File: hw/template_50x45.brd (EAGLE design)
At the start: 50 x 45 mm, 23 parts, among them J1 GROVE-4P-2.0-3470130P1, J2 GROVE-4P-2.0-3470130P1

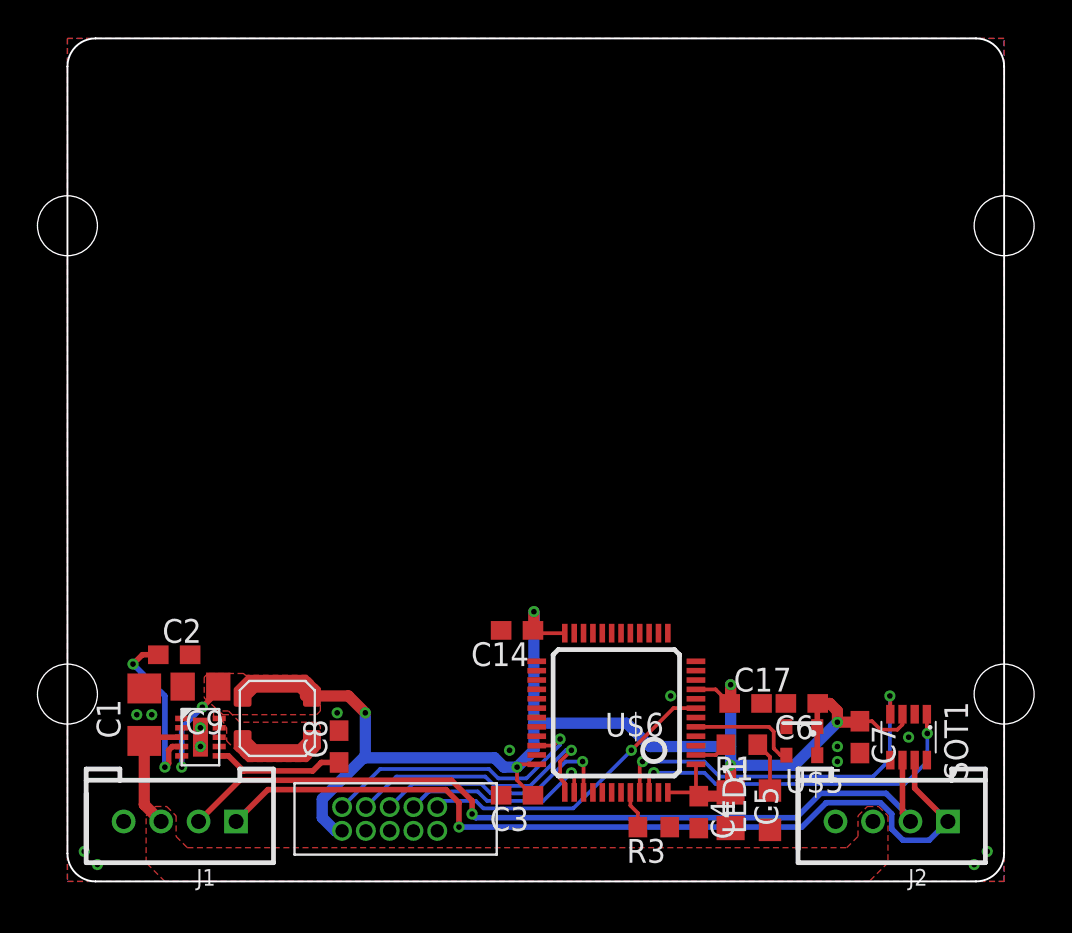
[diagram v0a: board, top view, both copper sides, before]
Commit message: Updated to R2P Eagle libraries
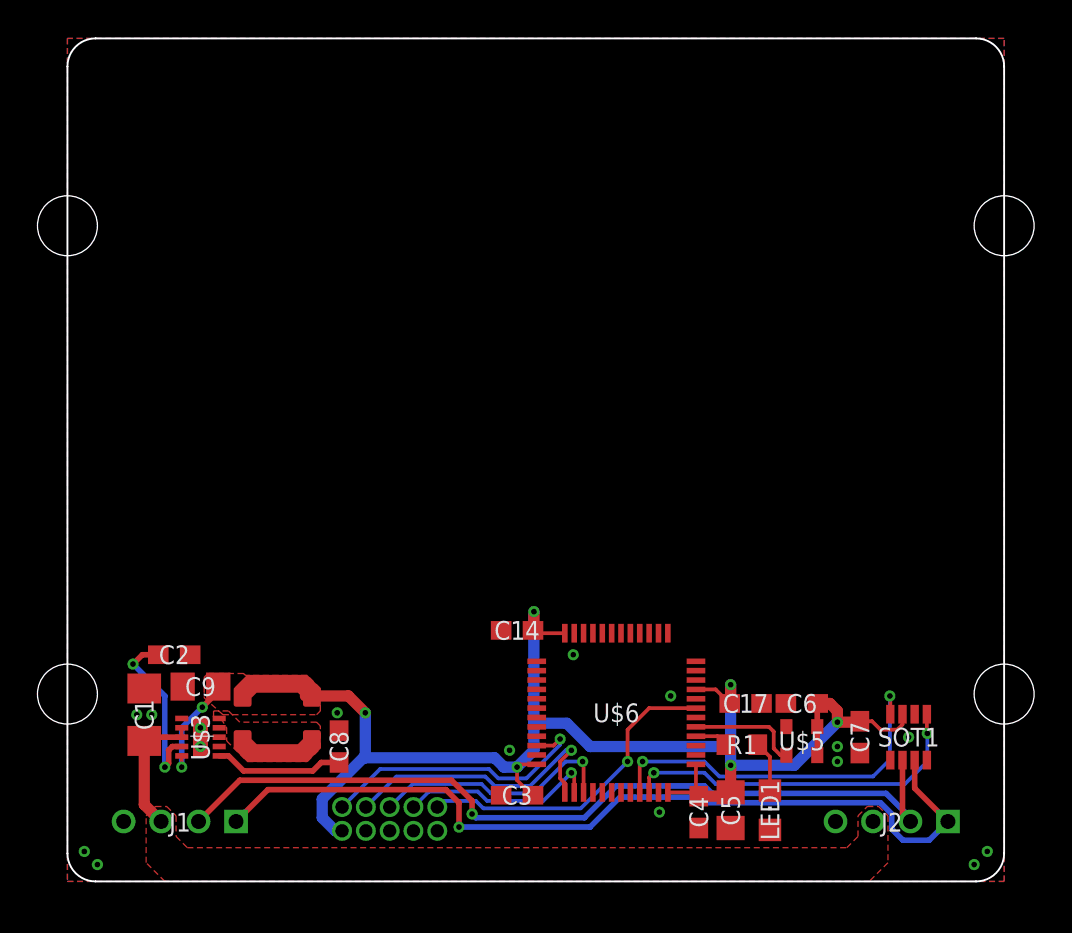
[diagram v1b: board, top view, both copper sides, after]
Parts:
- removed R3: 10k, rcl:R0603
- C1: value (none) -> 1u; device rcl:C1206 -> r2p_rcl:C1206
- C14, C17, C2, C3, C4, C6, C7, C8: device rcl:C0603 -> r2p_rcl:C0603
- C5: device rcl:C0805 -> r2p_rcl:C0805
- C9: value (none) -> 10u; device rcl:C0805 -> r2p_rcl:C0805
- J1, J2: value GROVE-4P-2.0-3470130P1 -> R2P_BUS-VERTICAL; device OPL Eagle Library:4P-2.0 -> r2p_connector:OPL-EAGLE-LIBRARY_4P-2.0
- LED1: device led:CHIPLED_0805 -> r2p_led:CHIPLED_0805
- R1: device rcl:R0603 -> r2p_rcl:R0603
- SOT1: device maxim:SOT23-8L -> r2p_ic:SOT23-8L
- U$2: device coilcraft:LPS4018 -> r2p_rcl:COILCRAFT_LPS4018
- U$3: device maxim:TDFN-10 -> r2p_ic:TDFN-10
- U$4: value FTSH-105TH -> JTAG-TH; device samtec:FTSH-105-TH -> r2p_connector:SAMTEC_FTSH-105-TH
- U$5: value ASD -> ABRACON_ASD; device abracon:2.5X2 -> r2p_ic:ABRACON_2.5X2
- U$6: value STM32F303C -> STM32F303CTX; device st:LQFP48 -> r2p_ic:LQFP48
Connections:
- net VIN renamed +VBUS
- removed net BOOT0: R3.2, U$6.44
- net GND: now also U$6.44; no longer R3.1
- net LED1: now also U$6.4; no longer U$6.2
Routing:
- net BOOT0: track 2.02 -> 0.00 mm
- net NRST: track 16.3 -> 17.3 mm

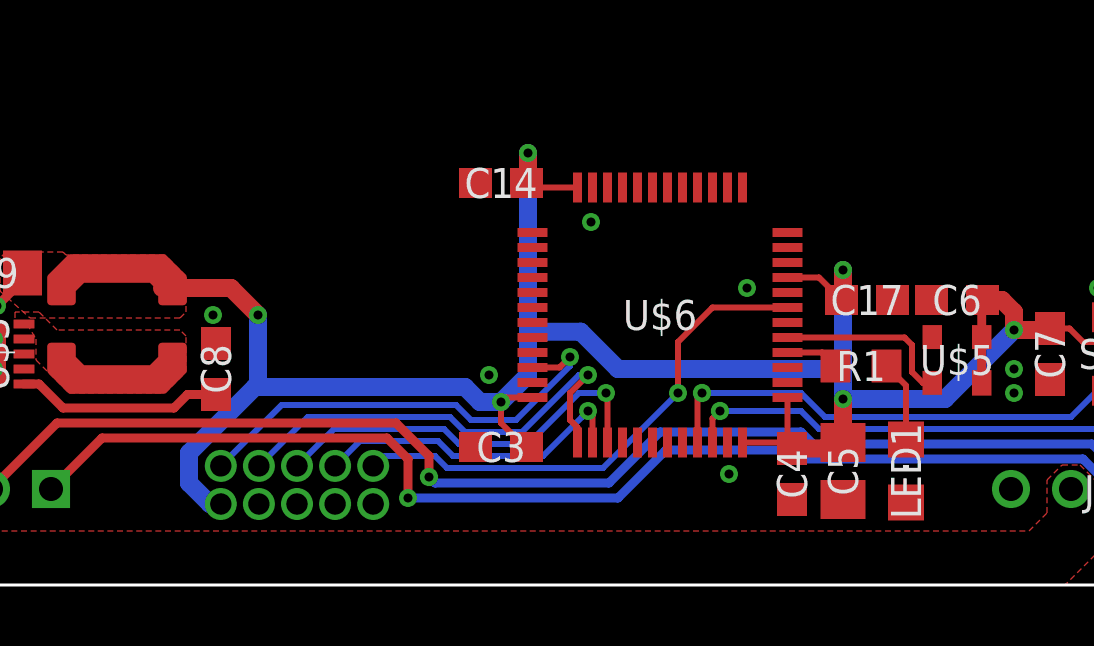
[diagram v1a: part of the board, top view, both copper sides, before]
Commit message: Approved DRU false warnings
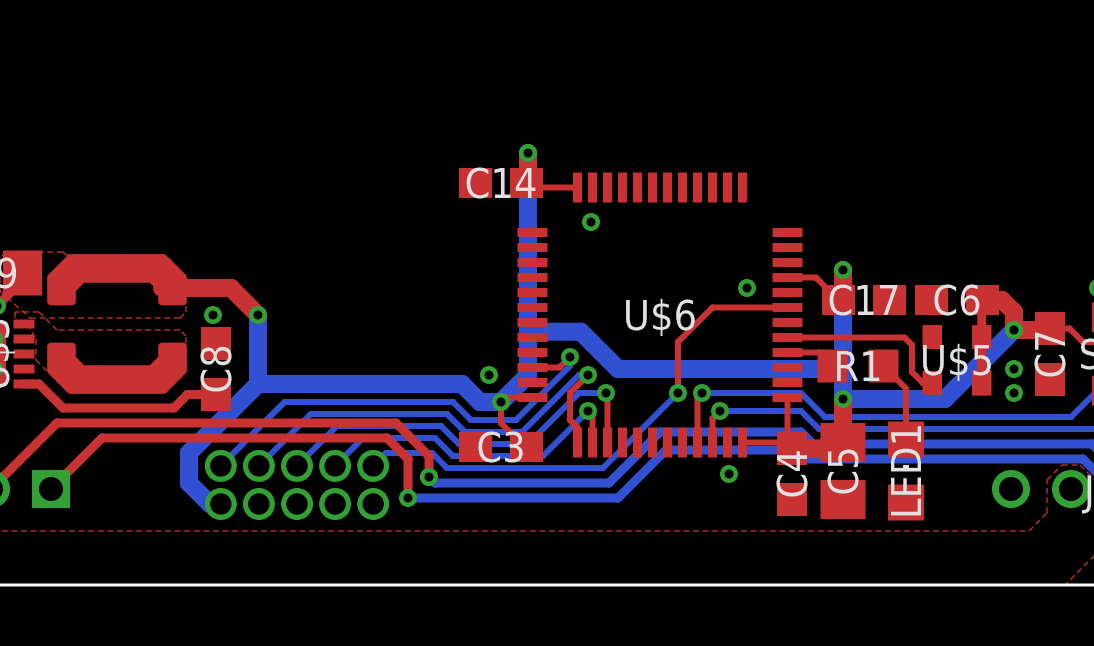
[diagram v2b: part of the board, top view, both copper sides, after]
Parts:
- moved C17 0.10 mm to (36.1, 9.50)
- moved R1 0.10 mm to (35.9, 7.30)

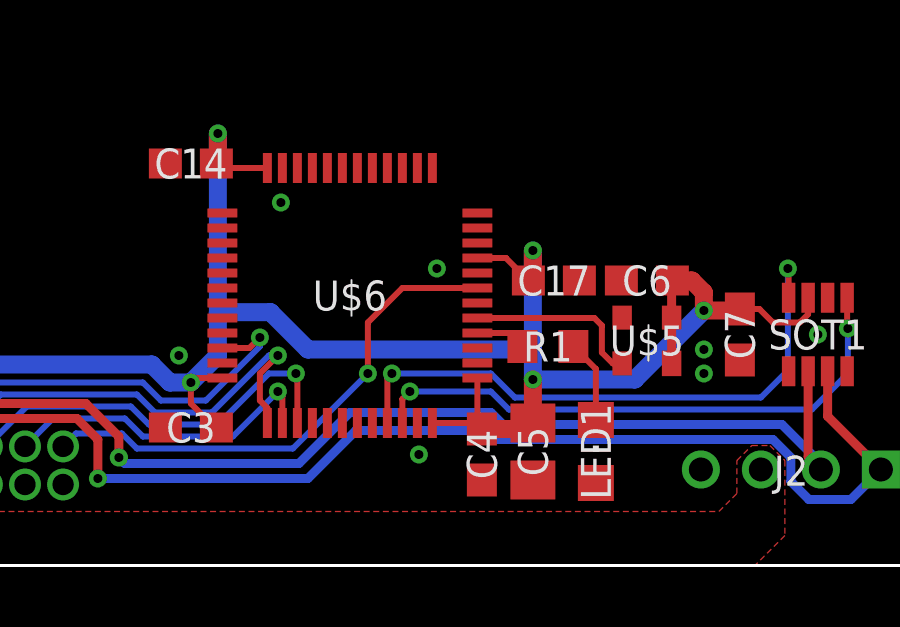
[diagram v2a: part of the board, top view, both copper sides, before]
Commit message: Updated keepout
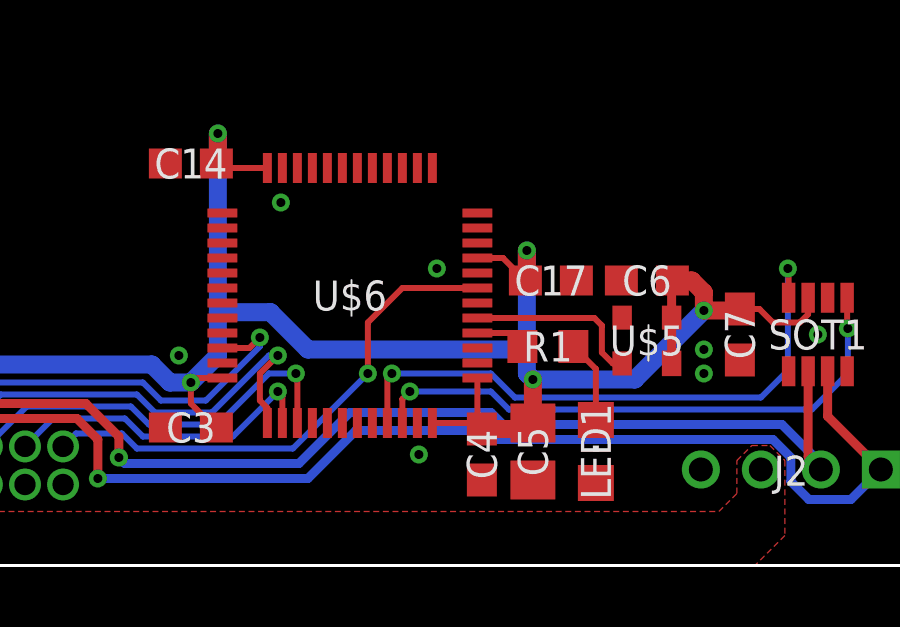
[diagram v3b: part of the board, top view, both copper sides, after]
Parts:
- U$2: value LPS4018 -> (none)
- moved C17 0.10 mm to (36.0, 9.50)
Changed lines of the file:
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@@
 <elements>
 <element name="C6" library="r2p_rcl" package="C0603" value="10n" x="39.2" y="9.5" rot="R180"/>
-<element name="C17" library="r2p_rcl" package="C0603" value="100n" x="36.1" y="9.5"/>
+<element name="C17" library="r2p_rcl" package="C0603" value="100n" x="36" y="9.5"/>
 <element name="C14" library="r2p_rcl" package="C0603" value="100n" x="24" y="13.4" rot="R180"/>
 <element name="C4" library="r2p_rcl" package="C0603" value="100n" x="33.7" y="3.7" rot="R270"/>
@@
 <element name="U$4" library="r2p_connector" package="SAMTEC_FTSH-105-TH" value="JTAG-TH" x="17.2" y="2.7"/>
 <element name="J2" library="r2p_connector" package="OPL-EAGLE-LIBRARY_4P-2.0" value="R2P_BUS-VERTICAL" x="44" y="3.2" rot="R180"/>
-<element name="U$2" library="r2p_rcl" package="COILCRAFT_LPS4018" value="LPS4018" x="11.2" y="8.7" rot="R90"/>
+<element name="U$2" library="r2p_rcl" package="COILCRAFT_LPS4018" value="" x="11.2" y="8.7" rot="R90"/>
 <element name="C1" library="r2p_rcl" package="C1206" value="1u" x="4.1" y="8.9" rot="R90"/>
 <element name="C2" library="r2p_rcl" package="C0603" value="1u" x="5.7" y="12.1"/>
@@
 <wire x1="24.85" y1="13.25" x2="24.85" y2="13.4" width="0.2" layer="1"/>
 <wire x1="8.2" y1="10.55" x2="8.05" y2="10.4" width="0.6" layer="1"/>
-<wire x1="33.55" y1="10.25" x2="34.5" y2="10.25" width="0.2" layer="1"/>
-<wire x1="34.5" y1="10.25" x2="35.25" y2="9.5" width="0.2" layer="1"/>
+<wire x1="33.55" y1="10.25" x2="34.4" y2="10.25" width="0.2" layer="1"/>
+<wire x1="34.4" y1="10.25" x2="35.15" y2="9.5" width="0.2" layer="1"/>
 <wire x1="40.025" y1="8.2625" x2="40.025" y2="9.475" width="0.3" layer="1"/>
 <wire x1="40.025" y1="9.475" x2="40.05" y2="9.5" width="0.3" layer="1"/>
@@
 <wire x1="35.4" y1="6.2" x2="38.8" y2="6.2" width="0.6" layer="16"/>
 <wire x1="38.8" y1="6.2" x2="41.1" y2="8.5" width="0.6" layer="16"/>
-<via x="35.4" y="10.5" extent="1-16" drill="0.3"/>
-<wire x1="35.4" y1="6.2" x2="35.4" y2="7.2" width="0.6" layer="16"/>
-<wire x1="35.4" y1="7.2" x2="35.4" y2="10.5" width="0.6" layer="16"/>
-<wire x1="35.4" y1="10.5" x2="35.4" y2="9.65" width="0.6" layer="1"/>
-<wire x1="35.4" y1="9.65" x2="35.25" y2="9.5" width="0.6" layer="1"/>
+<via x="35.2" y="10.5" extent="1-16" drill="0.3"/>
+<wire x1="35.2" y1="7.2" x2="35.2" y2="10.5" width="0.6" layer="16"/>
+<wire x1="35.2" y1="10.5" x2="35.2" y2="9.55" width="0.6" layer="1"/>
+<wire x1="35.2" y1="9.55" x2="35.15" y2="9.5" width="0.6" layer="1"/>
 <via x="24.9" y="14.4" extent="1-16" drill="0.3"/>
 <wire x1="24.85" y1="13.25" x2="24.9" y2="13.3" width="0.6" layer="1"/>
@@
 <wire x1="24.9" y1="8.443496875" x2="26.656503125" y2="8.443496875" width="0.6" layer="16"/>
 <wire x1="26.656503125" y1="8.443496875" x2="27.9" y2="7.2" width="0.6" layer="16"/>
-<wire x1="27.9" y1="7.2" x2="35.4" y2="7.2" width="0.6" layer="16"/>
+<wire x1="27.9" y1="7.2" x2="35.2" y2="7.2" width="0.6" layer="16"/>
 <wire x1="15.9" y1="6.7" x2="13.6" y2="4.4" width="0.6" layer="16"/>
 <wire x1="25.05" y1="6.25" x2="24.15" y2="6.25" width="0.2" layer="1"/>
 <wire x1="24.15" y1="6.25" x2="24" y2="6.1" width="0.2" layer="1"/>
 <wire x1="26.55" y1="13.25" x2="25" y2="13.25" width="0.2" layer="1"/>
+<wire x1="35.2" y1="7.2" x2="35.2" y2="6.4" width="0.6" layer="16"/>
+<wire x1="35.2" y1="6.4" x2="35.4" y2="6.2" width="0.6" layer="16"/>
 </signal>
 <signal name="JTMS">
